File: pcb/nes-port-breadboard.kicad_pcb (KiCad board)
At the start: 2 copper layers, 38.1 x 38.1 mm, 2 parts, among them J1 Conn_01x07, J2 NES_Port_Male

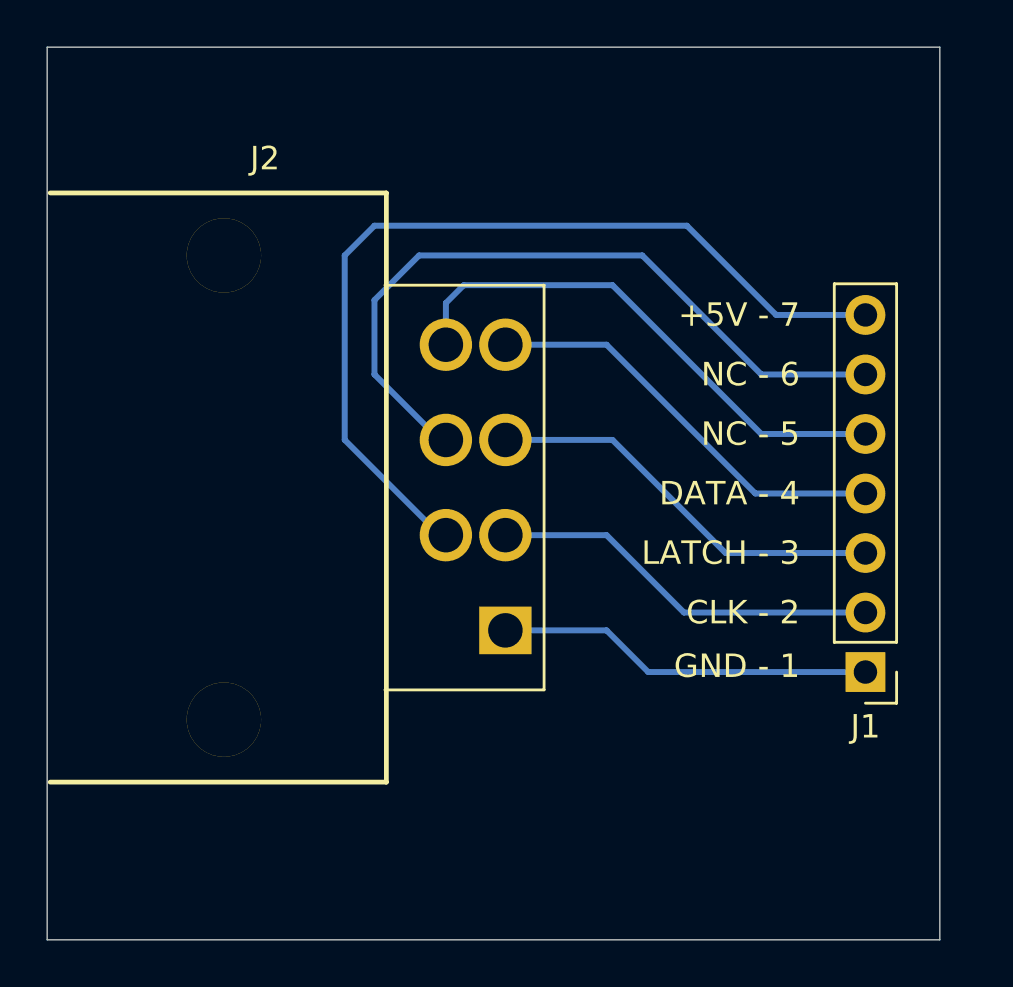
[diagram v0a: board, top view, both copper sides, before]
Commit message: Update mounting holes
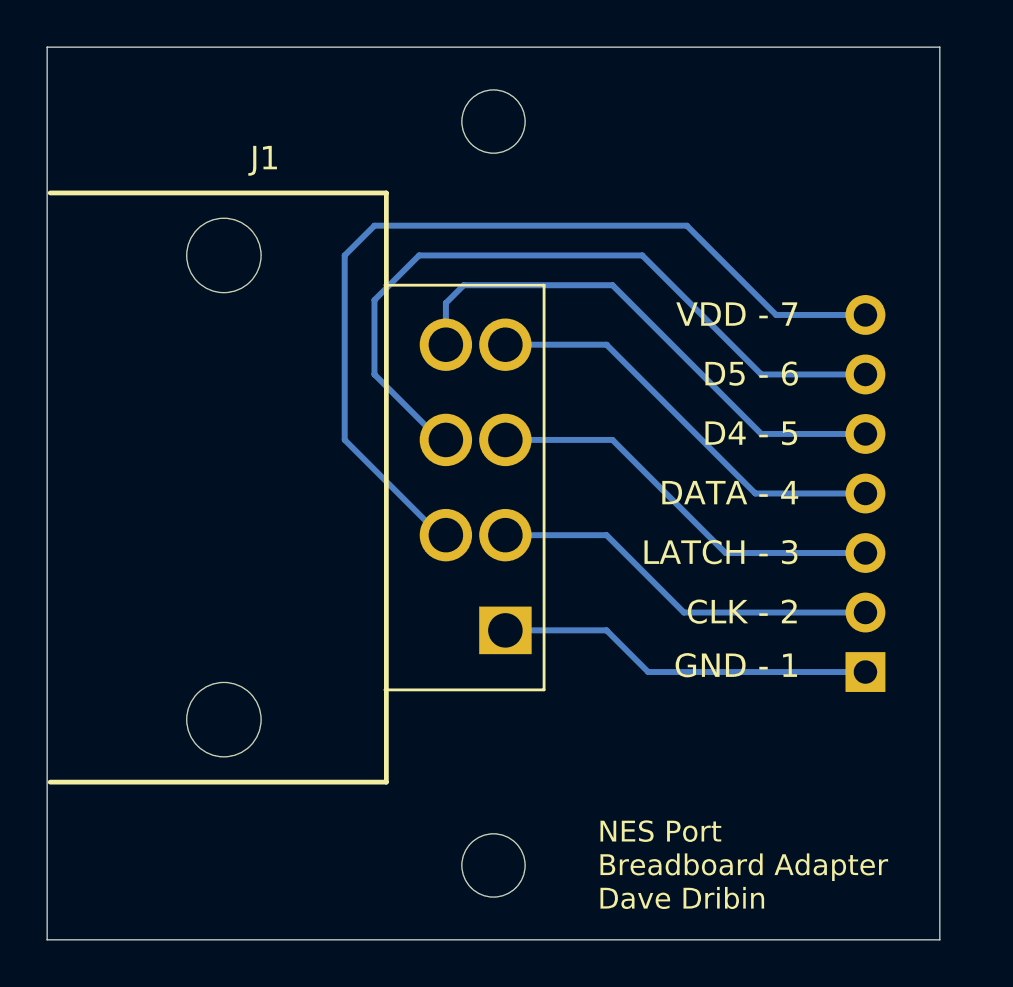
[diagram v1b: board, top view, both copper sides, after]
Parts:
- added REF**: MountingHole_2.7mm_M2.5, MountingHole:MountingHole_2.7mm_M2.5, F.Cu at (146.1, 123.8)
- added REF**: MountingHole_2.7mm_M2.5, MountingHole:MountingHole_2.7mm_M2.5, F.Cu at (146.1, 92.1)
- J2: renamed from J1; moved to B.Cu
- turned J2 to 0 degrees
- renumbered J2 to J1
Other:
- board text added: "D4 - 5"
- board text added: "D5 - 6"
- board text added: "NES Port Breadboard Adapter Dave Dribin"
- board text added: "VDD - 7"
- board text added: "Version 1.0"
- board text removed: "+5V - 7"
- board text removed: "NC - 5"
- board text removed: "NC - 6"

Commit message: Update dimensions
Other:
- board text added: "D3 - 6"
- board text removed: "D5 - 6"
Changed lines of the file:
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@@
       (effects (font (size 1 1) (thickness 0.15)))
     )
+    (fp_circle (center 0 0) (end 2.95 0) (layer F.CrtYd) (width 0.05))
+    (fp_circle (center 0 0) (end 2.7 0) (layer Cmts.User) (width 0.15))
     (fp_text user %R (at 0.3 0) (layer F.Fab) hide
       (effects (font (size 1 1) (thickness 0.15)))
     )
-    (fp_circle (center 0 0) (end 2.7 0) (layer Cmts.User) (width 0.15))
-    (fp_circle (center 0 0) (end 2.95 0) (layer F.CrtYd) (width 0.05))
     (pad 1 np_thru_hole circle (at 0 0) (size 2.7 2.7) (drill 2.7) (layers *.Cu *.Mask))
   )
@@
       (effects (font (size 1 1) (thickness 0.15)))
     )
+    (fp_circle (center 0 0) (end 2.95 0) (layer F.CrtYd) (width 0.05))
+    (fp_circle (center 0 0) (end 2.7 0) (layer Cmts.User) (width 0.15))
     (fp_text user %R (at 0.3 0) (layer F.Fab) hide
       (effects (font (size 1 1) (thickness 0.15)))
     )
-    (fp_circle (center 0 0) (end 2.7 0) (layer Cmts.User) (width 0.15))
-    (fp_circle (center 0 0) (end 2.95 0) (layer F.CrtYd) (width 0.05))
     (pad 1 np_thru_hole circle (at 0 0) (size 2.7 2.7) (drill 2.7) (layers *.Cu *.Mask))
   )
@@
       (effects (font (size 1 1) (thickness 0.15)))
     )
+    (fp_line (start -20.4724 -12.446) (end -6.2484 -12.446) (layer F.Fab) (width 0.1016))
+    (fp_line (start -17.4752 14.859) (end -15.2146 14.859) (layer F.Fab) (width 0.1016))
+    (fp_line (start -17.4752 12.446) (end -17.4752 14.859) (layer F.Fab) (width 0.1016))
+    (fp_line (start -15.2146 14.859) (end -15.2146 12.446) (layer F.Fab) (width 0.1016))
+    (fp_line (start -15.2146 -14.859) (end -15.2146 -12.446) (layer F.Fab) (width 0.1016))
+    (fp_line (start -17.4752 -14.859) (end -15.2146 -14.859) (layer F.Fab) (width 0.1016))
+    (fp_line (start -17.4752 -12.446) (end -17.4752 -14.859) (layer F.Fab) (width 0.1016))
+    (fp_line (start -6.2484 -12.446) (end -6.2484 12.446) (layer F.Fab) (width 0.1016))
+    (fp_line (start -20.4724 -12.446) (end -20.4724 12.446) (layer F.Fab) (width 0.1016))
+    (fp_line (start -20.447 -12.573) (end -6.096 -12.573) (layer F.SilkS) (width 0.2032))
+    (fp_line (start -6.2484 12.446) (end -20.4724 12.446) (layer F.Fab) (width 0.1016))
+    (fp_line (start -6.223 -8.001) (end 0 -8.001) (layer F.Fab) (width 0.12))
+    (fp_line (start -6.223 8.001) (end 0 8.001) (layer F.Fab) (width 0.12))
+    (fp_line (start 0 -8.001) (end 0 8.001) (layer F.Fab) (width 0.12))
+    (fp_line (start -6.096 -12.573) (end -6.096 12.573) (layer F.SilkS) (width 0.2032))
+    (fp_line (start -6.096 12.573) (end -20.447 12.573) (layer F.SilkS) (width 0.2032))
+    (fp_line (start -6.1595 -8.636) (end 0.635 -8.636) (layer F.SilkS) (width 0.12))
+    (fp_line (start 0.635 -8.636) (end 0.635 8.636) (layer F.SilkS) (width 0.12))
     (fp_line (start 0.635 8.636) (end -6.1595 8.636) (layer F.SilkS) (width 0.12))
-    (fp_line (start 0.635 -8.636) (end 0.635 8.636) (layer F.SilkS) (width 0.12))
-    (fp_line (start -6.1595 -8.636) (end 0.635 -8.636) (layer F.SilkS) (width 0.12))
-    (fp_line (start -6.096 12.573) (end -20.447 12.573) (layer F.SilkS) (width 0.2032))
-    (fp_line (start -6.096 -12.573) (end -6.096 12.573) (layer F.SilkS) (width 0.2032))
-    (fp_line (start 0 -8.001) (end 0 8.001) (layer F.Fab) (width 0.12))
-    (fp_line (start -6.223 8.001) (end 0 8.001) (layer F.Fab) (width 0.12))
-    (fp_line (start -6.223 -8.001) (end 0 -8.001) (layer F.Fab) (width 0.12))
-    (fp_line (start -6.2484 12.446) (end -20.4724 12.446) (layer F.Fab) (width 0.1016))
-    (fp_line (start -20.447 -12.573) (end -6.096 -12.573) (layer F.SilkS) (width 0.2032))
-    (fp_line (start -20.4724 -12.446) (end -20.4724 12.446) (layer F.Fab) (width 0.1016))
-    (fp_line (start -6.2484 -12.446) (end -6.2484 12.446) (layer F.Fab) (width 0.1016))
-    (fp_line (start -17.4752 -12.446) (end -17.4752 -14.859) (layer F.Fab) (width 0.1016))
-    (fp_line (start -17.4752 -14.859) (end -15.2146 -14.859) (layer F.Fab) (width 0.1016))
-    (fp_line (start -15.2146 -14.859) (end -15.2146 -12.446) (layer F.Fab) (width 0.1016))
-    (fp_line (start -15.2146 14.859) (end -15.2146 12.446) (layer F.Fab) (width 0.1016))
-    (fp_line (start -17.4752 12.446) (end -17.4752 14.859) (layer F.Fab) (width 0.1016))
-    (fp_line (start -17.4752 14.859) (end -15.2146 14.859) (layer F.Fab) (width 0.1016))
-    (fp_line (start -20.4724 -12.446) (end -6.2484 -12.446) (layer F.Fab) (width 0.1016))
     (pad 4 thru_hole circle (at -1.016 -6.096) (size 2.2352 2.2352) (drill 1.4732) (layers *.Cu *.Mask)
       (net 4 "Net-(J1-Pad4)"))
@@
       (effects (font (size 1 1) (thickness 0.15)) (justify mirror))
     )
+    (fp_line (start 1.8 1.8) (end -1.8 1.8) (layer B.CrtYd) (width 0.05))
+    (fp_line (start 1.8 -17.05) (end 1.8 1.8) (layer B.CrtYd) (width 0.05))
+    (fp_line (start -1.8 -17.05) (end 1.8 -17.05) (layer B.CrtYd) (width 0.05))
+    (fp_line (start -1.8 1.8) (end -1.8 -17.05) (layer B.CrtYd) (width 0.05))
+    (fp_line (start -1.33 1.33) (end 0 1.33) (layer B.SilkS) (width 0.12))
+    (fp_line (start -1.33 0) (end -1.33 1.33) (layer B.SilkS) (width 0.12))
+    (fp_line (start -1.33 -1.27) (end 1.33 -1.27) (layer B.SilkS) (width 0.12))
+    (fp_line (start 1.33 -1.27) (end 1.33 -16.57) (layer B.SilkS) (width 0.12))
+    (fp_line (start -1.33 -1.27) (end -1.33 -16.57) (layer B.SilkS) (width 0.12))
+    (fp_line (start -1.33 -16.57) (end 1.33 -16.57) (layer B.SilkS) (width 0.12))
+    (fp_line (start -1.27 0.635) (end -0.635 1.27) (layer B.Fab) (width 0.1))
+    (fp_line (start -1.27 -16.51) (end -1.27 0.635) (layer B.Fab) (width 0.1))
+    (fp_line (start 1.27 -16.51) (end -1.27 -16.51) (layer B.Fab) (width 0.1))
+    (fp_line (start 1.27 1.27) (end 1.27 -16.51) (layer B.Fab) (width 0.1))
     (fp_line (start -0.635 1.27) (end 1.27 1.27) (layer B.Fab) (width 0.1))
-    (fp_line (start 1.27 1.27) (end 1.27 -16.51) (layer B.Fab) (width 0.1))
-    (fp_line (start 1.27 -16.51) (end -1.27 -16.51) (layer B.Fab) (width 0.1))
-    (fp_line (start -1.27 -16.51) (end -1.27 0.635) (layer B.Fab) (width 0.1))
-    (fp_line (start -1.27 0.635) (end -0.635 1.27) (layer B.Fab) (width 0.1))
-    (fp_line (start -1.33 -16.57) (end 1.33 -16.57) (layer B.SilkS) (width 0.12))
-    (fp_line (start -1.33 -1.27) (end -1.33 -16.57) (layer B.SilkS) (width 0.12))
-    (fp_line (start 1.33 -1.27) (end 1.33 -16.57) (layer B.SilkS) (width 0.12))
-    (fp_line (start -1.33 -1.27) (end 1.33 -1.27) (layer B.SilkS) (width 0.12))
-    (fp_line (start -1.33 0) (end -1.33 1.33) (layer B.SilkS) (width 0.12))
-    (fp_line (start -1.33 1.33) (end 0 1.33) (layer B.SilkS) (width 0.12))
-    (fp_line (start -1.8 1.8) (end -1.8 -17.05) (layer B.CrtYd) (width 0.05))
-    (fp_line (start -1.8 -17.05) (end 1.8 -17.05) (layer B.CrtYd) (width 0.05))
-    (fp_line (start 1.8 -17.05) (end 1.8 1.8) (layer B.CrtYd) (width 0.05))
-    (fp_line (start 1.8 1.8) (end -1.8 1.8) (layer B.CrtYd) (width 0.05))
     (fp_text user %R (at 0 -7.62 270) (layer B.Fab)
       (effects (font (size 1 1) (thickness 0.15)) (justify mirror))
@@
   )
   (dimension 38.1 (width 0.15) (layer Dwgs.User)
-    (gr_text "1.5000 in" (at 146.05 85.06) (layer Dwgs.User)
+    (gr_text "1.5000 in" (at 146.05 130.84) (layer Dwgs.User)
       (effects (font (size 1 1) (thickness 0.15)))
     )
-    (feature1 (pts (xy 165.1 88.9) (xy 165.1 85.773579)))
-    (feature2 (pts (xy 127 88.9) (xy 127 85.773579)))
-    (crossbar (pts (xy 127 86.36) (xy 165.1 86.36)))
-    (arrow1a (pts (xy 165.1 86.36) (xy 163.973496 86.946421)))
-    (arrow1b (pts (xy 165.1 86.36) (xy 163.973496 85.773579)))
-    (arrow2a (pts (xy 127 86.36) (xy 128.126504 86.946421)))
-    (arrow2b (pts (xy 127 86.36) (xy 128.126504 85.773579)))
+    (feature1 (pts (xy 165.1 127) (xy 165.1 130.126421)))
+    (feature2 (pts (xy 127 127) (xy 127 130.126421)))
+    (crossbar (pts (xy 127 129.54) (xy 165.1 129.54)))
+    (arrow1a (pts (xy 165.1 129.54) (xy 163.973496 130.126421)))
+    (arrow1b (pts (xy 165.1 129.54) (xy 163.973496 128.953579)))
+    (arrow2a (pts (xy 127 129.54) (xy 128.126504 130.126421)))
+    (arrow2b (pts (xy 127 129.54) (xy 128.126504 128.953579)))
   )
   (dimension 38.1 (width 0.15) (layer Dwgs.User)
@@
     (effects (font (size 1 1) (thickness 0.15)) (justify right))
   )
-  (gr_text "D5 - 6" (at 159.131 102.87) (layer F.SilkS)
+  (gr_text "D3 - 6" (at 159.131 102.87) (layer F.SilkS)
     (effects (font (size 1 1) (thickness 0.15)) (justify right))
   )

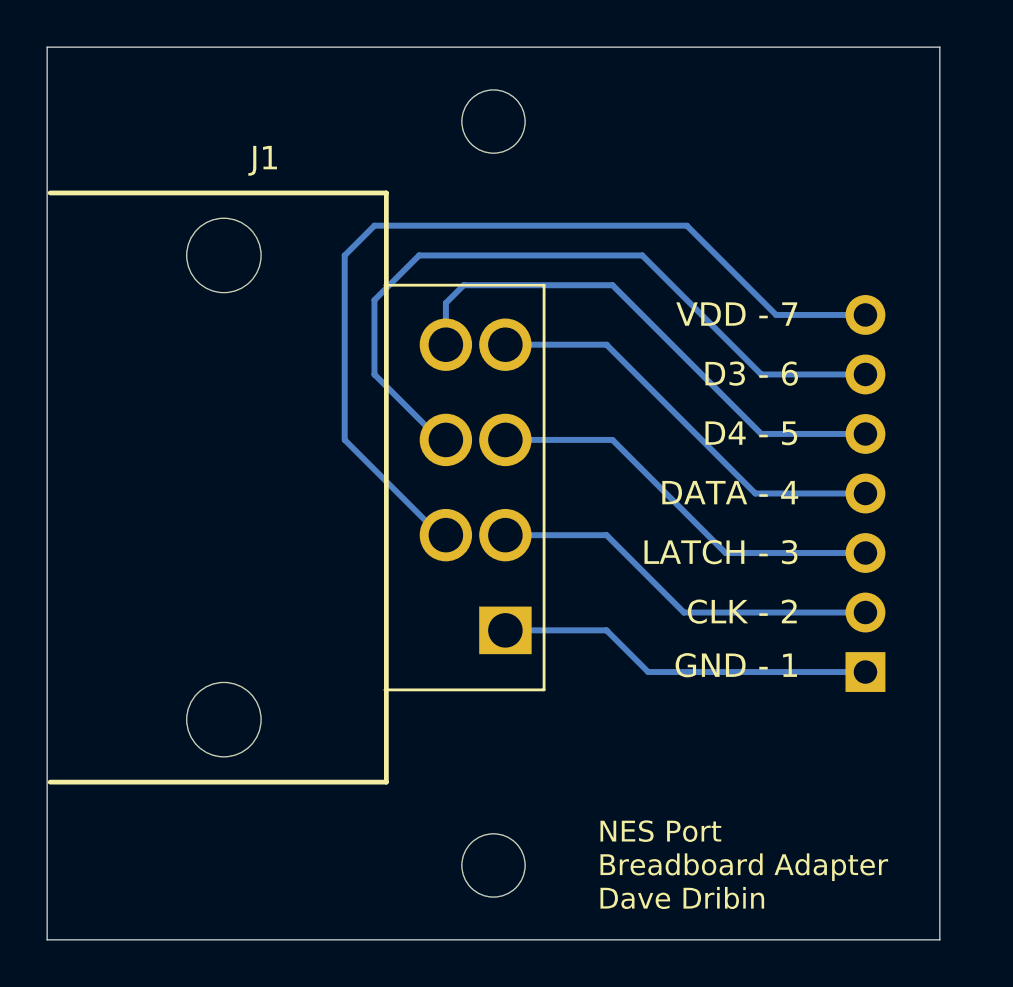
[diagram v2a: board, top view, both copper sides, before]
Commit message: Tweak tracks. Update Gerber and drill settings. Add mounting hole labels.
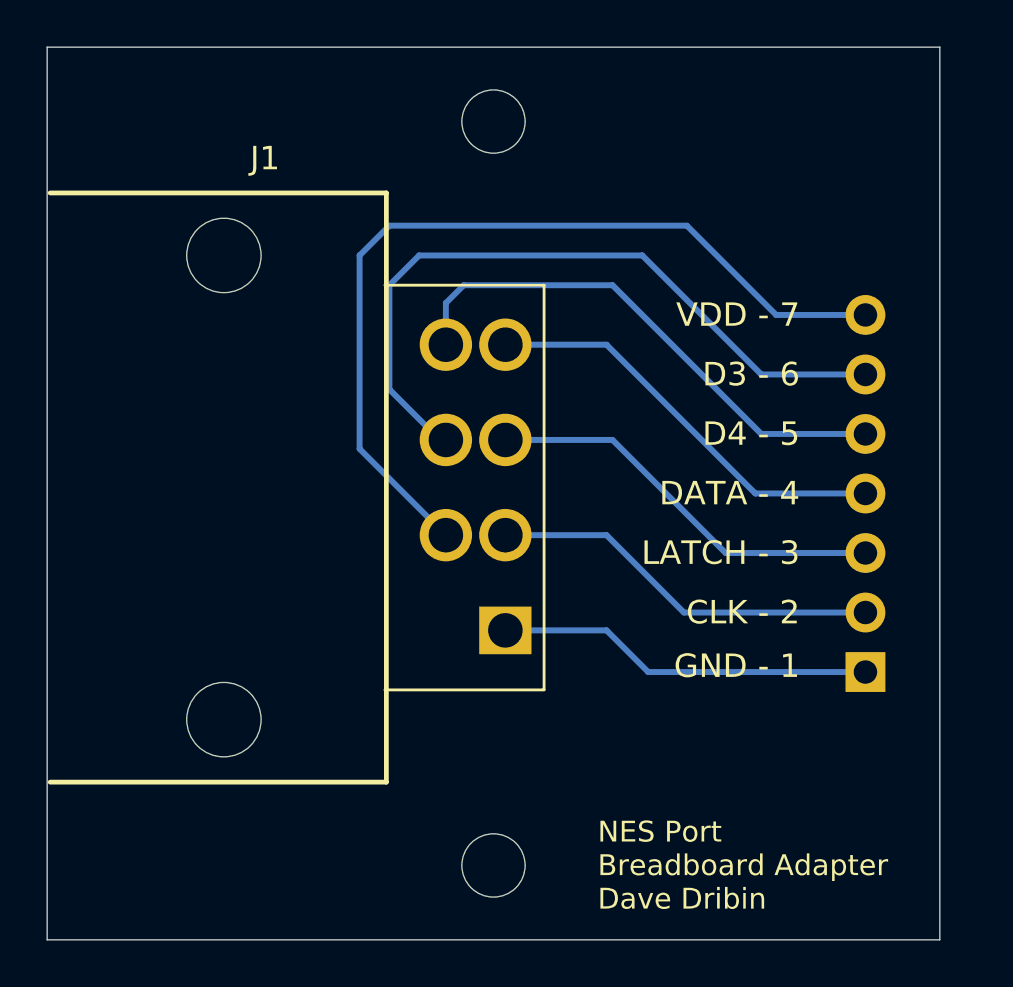
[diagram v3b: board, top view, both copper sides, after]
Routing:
- net Net-(J1-Pad7): track 38.3 -> 37.3 mm
- net Net-(J1-Pad6): track 31.3 -> 30.8 mm
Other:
- board text added: "M2.5"

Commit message: Make NES port holes bigger. Shrink board to 1.4x1.4 inches
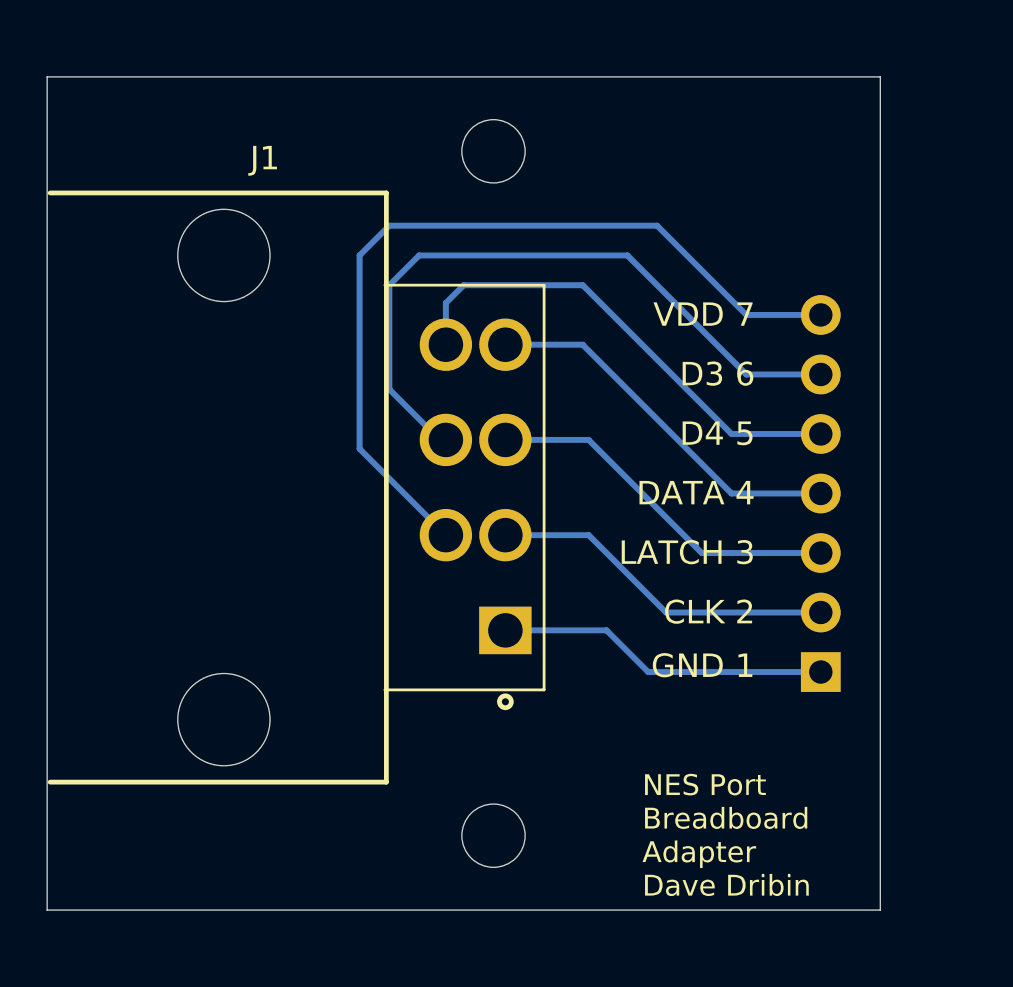
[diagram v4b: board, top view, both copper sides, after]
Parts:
- removed REF** (x2): MountingHole_2.7mm_M2.5, MountingHole:MountingHole_2.7mm_M2.5
- added H1: MountingHole, MountingHole:MountingHole_2.7mm_M2.5, F.Cu at (146.1, 93.3)
- added H2: MountingHole, MountingHole:MountingHole_2.7mm_M2.5, F.Cu at (146.1, 122.6)
- moved J2 1.91 mm to (160.0, 115.6)
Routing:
- net Net-(J1-Pad6): track 30.8 -> 28.9 mm
- net Net-(J1-Pad7): track 37.3 -> 35.4 mm
- net Net-(J1-Pad5): track 22.6 -> 20.7 mm
- net Net-(J1-Pad4): track 18.0 -> 16.1 mm
- net Net-(J1-Pad2): track 16.7 -> 14.8 mm
- net Net-(J1-Pad1): track 16.1 -> 14.2 mm
- net Net-(J1-Pad3): track 17.4 -> 15.7 mm
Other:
- board size 38.1 x 38.1 mm -> 35.6 x 35.6 mm
- board text added: "CLK 2"
- board text added: "D3 6"
- board text added: "D4 5"
- board text added: "DATA 4"
- board text added: "GND 1"
- board text added: "LATCH 3"
- board text added: "VDD 7"
- board text added: "Version 1.0.1"
- board text removed: "CLK - 2"
- board text removed: "D3 - 6"
- board text removed: "D4 - 5"
- board text removed: "DATA - 4"
- board text removed: "GND - 1"
- board text removed: "LATCH - 3"
- board text removed: "VDD - 7"
- board text removed: "Version 1.0"
